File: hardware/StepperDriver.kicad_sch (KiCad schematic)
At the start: 17 parts, among them J201 Conn_01x01, J202 Conn_01x01, J203 Conn_01x01, J204 Conn_01x01, U201 TMC2130-LA

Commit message: Update parts library
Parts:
- C201, C207: footprint Capacitor_SMD:C_0603_1608Metric -> V2_Capacitor_SMD:C_0603; symbol Device:C_Small -> V2_Device:C_0603_0u1; Mouser (none) -> 810-CGA3E2X7R1H104MA
- C202: footprint Capacitor_SMD:CP_Elec_6.3x5.8 -> V2_Capacitor_SMD:CP_Elec_6.3x5.8; symbol Device:C_Polarized_Small -> V2_Device:C_Polarized_6.3x5.8_1_47u; Mouser (none) -> 667-EEE-FK1V470P
- C203, C204: footprint Capacitor_SMD:C_1210_3225Metric -> V2_Capacitor_SMD:C_1210; symbol Device:C_Small -> V2_Device:C_1210_10u; Mouser (none) -> 810-CNA6P1X7R1H106K2; Rating (none) -> 50V
- C205: footprint Capacitor_SMD:C_0603_1608Metric -> V2_Capacitor_SMD:C_0603; symbol Device:C_Small -> V2_Device:C_0603_4u7; Mouser (none) -> 603-CC603KRX5R6BB475
- C206: footprint Capacitor_SMD:C_0603_1608Metric -> V2_Capacitor_SMD:C_0603; symbol Device:C_Small -> V2_Device:C_0603_0u470; Mouser (none) -> 603-CC0603JR6BB474
- C208: footprint Capacitor_SMD:C_0603_1608Metric -> V2_Capacitor_SMD:C_0603; symbol Device:C_Small -> V2_Device:C_0603_0u022; Mouser (none) -> 603-CC603KPX7R9BB223
- J201, J202, J203, J204: value Conn_01x01 -> WAGO 2065-100
- R201: footprint Resistor_SMD:R_0603_1608Metric -> V2_Resistor_SMD:R_0603; symbol Device:R_Small -> V2_Device:R_0603_2R2; Mouser (none) -> 71-RCS06032R20JNEA
- R202, R203: footprint Resistor_SMD:R_0805_2012Metric -> V2_Resistor_SMD:R_0805; symbol Device:R_Small -> V2_Device:R_0805_0R11; Mouser (none) -> 667-ERJ-6DSFR11V

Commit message: Update parts
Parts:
- C201, C207: Manufacturer (none) -> TDK; Product (none) -> CGA3E2X7R1H104M080AA
- C202: symbol V2_Device:C_Polarized_6.3x5.8_1_47u -> V2_Device:C_Polarized_6.3x5.8_47u; Manufacturer (none) -> Panasonic; Product (none) -> EEE-FK1V470P; Rating (none) -> 35V
- C203, C204: Manufacturer (none) -> TDK; Product (none) -> CNA6P1X7R1H106K250AE; Voltage (none) -> 50V
- C205: Manufacturer (none) -> YAGEO; Product (none) -> CC0603KRX5R6BB475
- C206: value 0u470 -> 0u47; symbol V2_Device:C_0603_0u470 -> V2_Device:C_0603_0u47; Manufacturer (none) -> YAGEO; Product (none) -> CC0603JRX7R6BB474
- C208: Manufacturer (none) -> YAGEO; Product (none) -> CC0603KPX7R9BB223
- D201: LCSC (none) -> C965555; Manufacturer (none) -> Worldsemi; Product (none) -> WS2812B-2020
- J201, J202, J203, J204: Manufacturer (none) -> WAGO; Product (none) -> 2065-100/998-403
- R201: Manufacturer (none) -> Vishay; Product (none) -> RCS06032R20JNEA; Rating (none) -> 500mW
- R202, R203: Manufacturer (none) -> Panasonic; Product (none) -> ERJ-6DSFR11V; Rating (none) -> 500mW
- U201: LCSC (none) -> C915795; Manufacturer (none) -> Analog Devices; Product (none) -> TMC2130-LA
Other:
- moved on the sheet: C205, C206, R201

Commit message: Refresh
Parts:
- C201, C207: Rating (none) -> 50V
- C203, C204: Voltage 50V -> (none)
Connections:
- net +24V renamed +28V
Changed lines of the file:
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@@
 			)
 		)
-		(property "Voltage" "50V"
-			(at 158.75 68.58 0)
-			(effects
-				(font
-					(size 1.27 1.27)
-				)
-				(hide yes)
-			)
-		)
 		(property "Product" "CNA6P1X7R1H106K250AE"
 			(at 158.75 67.31 0)
@@
 			)
 		)
-		(property "Sim.Enable" ""
-			(at 158.75 49.53 0)
-			(effects
-				(font
-					(size 1.27 1.27)
-				)
-				(hide yes)
-			)
-		)
 		(pin "1"
 		)
@@
 			)
 		)
-		(property "Sim.Enable" ""
-			(at 107.95 81.28 0)
-			(effects
-				(font
-					(size 1.27 1.27)
-				)
-				(hide yes)
-			)
-		)
 		(pin "1"
 		)
@@
 	)
 	(symbol
-		(lib_id "V2_power:+24V")
+		(lib_id "V2_power:+28V")
 		(at 139.7 88.9 90)
 		(unit 1)
@@
 			)
 		)
-		(property "Value" "+24V"
+		(property "Value" "+28V"
 			(at 135.89 88.8999 90)
 			(effects
@@
 			)
 		)
-		(property "Description" "Power symbol creates a global label with name \"+24V\""
+		(property "Description" ""
 			(at 139.7 88.9 0)
 			(effects
@@
 			)
 		)
-		(property "Sim.Enable" ""
-			(at 175.26 91.44 0)
-			(effects
-				(font
-					(size 1.27 1.27)
-				)
-				(hide yes)
-			)
-		)
 		(pin "1"
 		)
@@
 			)
 		)
-		(property "Voltage" "50V"
-			(at 170.18 68.58 0)
-			(effects
-				(font
-					(size 1.27 1.27)
-				)
-				(hide yes)
-			)
-		)
 		(property "Product" "CNA6P1X7R1H106K250AE"
 			(at 170.18 67.31 0)
@@
 			)
 		)
-		(property "Sim.Enable" ""
-			(at 170.18 49.53 0)
-			(effects
-				(font
-					(size 1.27 1.27)
-				)
-				(hide yes)
-			)
-		)
 		(pin "1"
 		)
@@
 			)
 		)
-		(property "Description" "Power symbol creates a global label with name \"GND\" , ground"
+		(property "Description" ""
 			(at 191.77 129.54 0)
 			(effects
@@
 			)
 		)
-		(property "Sim.Enable" ""
-			(at 157.48 160.02 0)
-			(effects
-				(font
-					(size 1.27 1.27)
-				)
-				(hide yes)
-			)
-		)
 		(pin "1"
 		)
@@
 			)
 		)
-		(property "Sim.Enable" ""
-			(at 124.46 49.53 0)
+		(property "Rating" "50V"
+			(at 124.46 72.39 0)
 			(effects
 				(font
@@
 			)
 		)
-		(property "Description" "Power symbol creates a global label with name \"GND\" , ground"
+		(property "Description" ""
 			(at 175.26 139.7 0)
 			(effects
@@
 			)
 		)
-		(property "Description" "Power symbol creates a global label with name \"+5V\""
+		(property "Description" ""
 			(at 165.1 156.21 0)
 			(effects
@@
 			)
 		)
-		(property "Description" "Power symbol creates a global label with name \"GND\" , ground"
+		(property "Description" ""
 			(at 191.77 127 0)
 			(effects
@@
 			)
 		)
-		(property "Sim.Enable" ""
-			(at 189.23 127 90)
-			(effects
-				(font
-					(size 1.27 1.27)
-				)
-				(hide yes)
-			)
-		)
 		(pin "1"
 		)
@@
 			)
 		)
-		(property "Description" "Power symbol creates a global label with name \"GND\" , ground"
+		(property "Description" ""
 			(at 124.46 52.07 0)
 			(effects
@@
 			)
 		)
-		(property "Sim.Enable" ""
-			(at 139.7 86.36 0)
+		(property "Rating" "50V"
+			(at 139.7 109.22 0)
 			(effects
 				(font
@@
 			)
 		)
-		(property "Description" "Power symbol creates a global label with name \"GND\" , ground"
+		(property "Description" ""
 			(at 170.18 52.07 0)
 			(effects
@@
 			)
 		)
-		(property "Description" "Power symbol creates a global label with name \"GND\" , ground"
+		(property "Description" ""
 			(at 139.7 104.14 0)
 			(effects
@@
 			)
 		)
-		(property "Description" "Power symbol creates a global label with name \"+3V3\""
+		(property "Description" ""
 			(at 139.7 81.28 0)
 			(effects
@@
 			)
 		)
-		(property "Description" "Power symbol creates a global label with name \"+3V3\""
+		(property "Description" ""
 			(at 124.46 46.99 0)
 			(effects
@@
 	)
 	(symbol
-		(lib_id "V2_power:+24V")
+		(lib_id "V2_power:+28V")
 		(at 139.7 91.44 90)
 		(unit 1)
@@
 			)
 		)
-		(property "Value" "+24V"
+		(property "Value" "+28V"
 			(at 135.89 91.4399 90)
 			(effects
@@
 			)
 		)
-		(property "Description" "Power symbol creates a global label with name \"+24V\""
+		(property "Description" ""
 			(at 139.7 91.44 0)
 			(effects
@@
 			)
 		)
-		(property "Description" "Power symbol creates a global label with name \"GND\" , ground"
+		(property "Description" ""
 			(at 120.65 83.82 0)
 			(effects
@@
 			)
 		)
-		(property "Sim.Enable" ""
-			(at 143.51 49.53 0)
-			(effects
-				(font
-					(size 1.27 1.27)
-				)
-				(hide yes)
-			)
-		)
 		(pin "1"
 		)
@@
 			)
 		)
-		(property "Sim.Enable" ""
-			(at 189.23 83.82 0)
-			(effects
-				(font
-					(size 1.27 1.27)
-				)
-				(hide yes)
-			)
-		)
 		(pin "1"
 		)
@@
 			)
 		)
-		(property "Sim.Enable" ""
-			(at 189.23 81.28 0)
-			(effects
-				(font
-					(size 1.27 1.27)
-				)
-				(hide yes)
-			)
-		)
 		(pin "1"
 		)
@@
 			)
 		)
-		(property "Description" "Power symbol creates a global label with name \"GND\" , ground"
+		(property "Description" ""
 			(at 139.7 106.68 0)
 			(effects
@@
 			)
 		)
-		(property "Description" "Power symbol creates a global label with name \"GND\" , ground"
+		(property "Description" ""
 			(at 107.95 83.82 0)
 			(effects
@@
 			)
 		)
-		(property "Sim.Enable" ""
-			(at 114.3 78.74 90)
-			(effects
-				(font
-					(size 1.27 1.27)
-				)
-				(hide yes)
-			)
-		)
 		(pin "1"
 		)
@@
 			)
 		)
-		(property "Sim.Enable" ""
-			(at 157.48 106.68 0)
-			(effects
-				(font
-					(size 1.27 1.27)
-				)
-				(hide yes)
-			)
-		)
 		(pin "13"
 		)
@@
 			)
 		)
-		(property "Sim.Enable" ""
-			(at 189.23 76.2 0)
-			(effects
-				(font
-					(size 1.27 1.27)
-				)
-				(hide yes)
-			)
-		)
 		(pin "1"
 		)
@@
 			)
 		)
-		(property "Sim.Enable" ""
-			(at 189.23 129.54 90)
-			(effects
-				(font
-					(size 1.27 1.27)
-				)
-				(hide yes)
-			)
-		)
 		(pin "1"
 		)
@@
 	)
 	(symbol
-		(lib_id "V2_power:+24V")
+		(lib_id "V2_power:+28V")
 		(at 170.18 46.99 0)
 		(unit 1)
@@
 			)
 		)
-		(property "Value" "+24V"
+		(property "Value" "+28V"
 			(at 170.18 41.91 0)
 			(effects
@@
 			)
 		)
-		(property "Description" "Power symbol creates a global label with name \"+24V\""
+		(property "Description" ""
 			(at 170.18 46.99 0)
 			(effects
@@
 			)
 		)
-		(property "Sim.Enable" ""
-			(at 120.65 81.28 0)
-			(effects
-				(font
-					(size 1.27 1.27)
-				)
-				(hide yes)
-			)
-		)
 		(pin "1"
 		)
@@
 			)
 		)
-		(property "Description" "Power symbol creates a global label with name \"GND\" , ground"
+		(property "Description" ""
 			(at 139.7 124.46 0)
 			(effects
@@
 			)
 		)
-		(property "Sim.Enable" ""
-			(at 189.23 73.66 0)
-			(effects
-				(font
-					(size 1.27 1.27)
-				)
-				(hide yes)
-			)
-		)
 		(pin "1"
 		)
@@
 			)
 		)
-		(property "Description" "Power symbol creates a global label with name \"GND\" , ground"
+		(property "Description" ""
 			(at 165.1 161.29 0)
 			(effects

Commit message: Update library
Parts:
- U201: footprint V2_Driver_Stepper:QFN36-5X6 -> V2_Package_DFN_QFN:QFN36-5X6
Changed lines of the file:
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@@
 			)
 		)
-		(property "Footprint" "V2_Driver_Stepper:QFN36-5X6"
+		(property "Footprint" "V2_Package_DFN_QFN:QFN36-5X6"
 			(at 158.75 150.114 0)
 			(effects

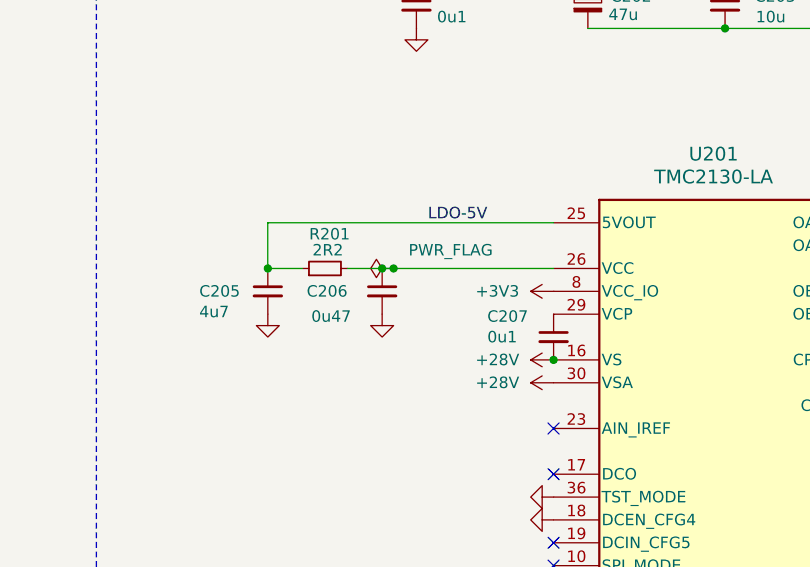
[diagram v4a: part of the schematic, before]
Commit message: Replace Order_Number
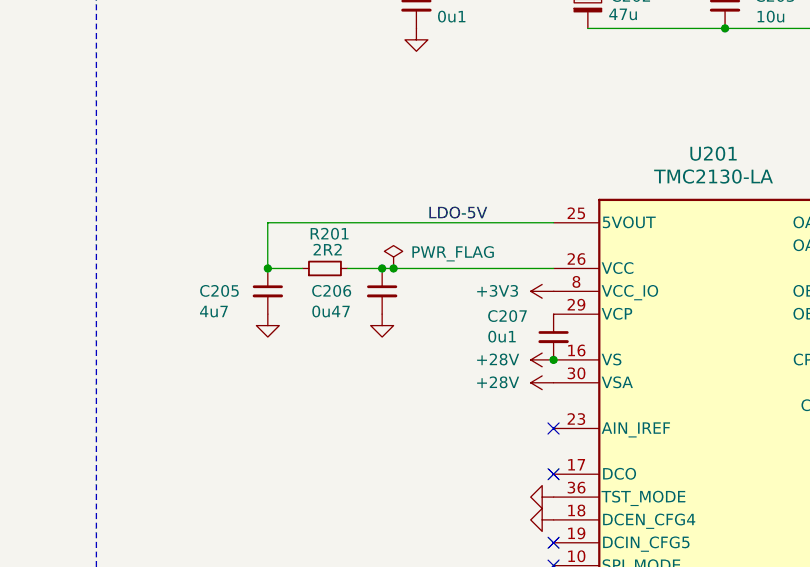
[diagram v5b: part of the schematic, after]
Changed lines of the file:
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@@
 	(title_block
 		(title "Stepper Driver")
-		(date "2025-10-27")
-		(rev "2")
+		(date "2026-02-10")
+		(rev "2026-02-10")
 		(company "Versio Duo")
 	)
@@
 		(dnp no)
 		(property "Reference" "C206"
-			(at 112.268 81.28 0)
+			(at 112.776 81.28 0)
 			(effects
 				(font
@@
 		)
 		(property "Value" "0u47"
-			(at 112.776 84.074 0)
+			(at 112.776 83.566 0)
 			(effects
 				(font
@@
 	(symbol
 		(lib_id "V2_power:PWR_FLAG")
-		(at 121.92 78.74 0)
+		(at 121.92 78.74 270)
 		(unit 1)
 		(exclude_from_sim no)
@@
 		(dnp no)
 		(property "Reference" "#FLG0201"
-			(at 121.92 76.835 0)
+			(at 123.825 78.74 0)
 			(effects
 				(font
@@
 		)
 		(property "Value" "PWR_FLAG"
-			(at 128.27 76.708 0)
+			(at 128.524 76.962 90)
 			(effects
 				(font

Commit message: Update Library
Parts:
- C201, C207: symbol V2_Device:C_0603_0u1 -> V2_Capacitor:0603_0u1
- C202: symbol V2_Device:C_Polarized_6.3x5.8_47u -> V2_Capacitor:Polarized_6.3x5.8_47u
- C203, C204: symbol V2_Device:C_1210_10u -> V2_Capacitor:1210_10u
- C205: symbol V2_Device:C_0603_4u7 -> V2_Capacitor:0603_4u7
- C206: symbol V2_Device:C_0603_0u47 -> V2_Capacitor:0603_0u47
- C208: symbol V2_Device:C_0603_0u022 -> V2_Capacitor:0603_0u022
- R201: symbol V2_Device:R_0603_2R2 -> V2_Resistor:0603_2R2
- R202, R203: symbol V2_Device:R_0805_0R11 -> V2_Resistor:0805_0R11

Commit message: Update
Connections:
- net LDO-5V renamed +5VOUT
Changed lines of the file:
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@@
 		)
 	)
-	(label "LDO-5V"
+	(label "+5VOUT"
 		(at 125.73 73.66 0)
 		(effects
@@
 		(on_board yes)
 		(dnp no)
-		(fields_autoplaced yes)
 		(property "Reference" "#PWR208"
 			(at 143.51 88.9 0)
@@
 		)
 		(property "Value" "+28V"
-			(at 135.89 88.8999 90)
-			(effects
-				(font
-					(size 1.27 1.27)
-				)
-				(justify left)
+			(at 133.35 88.8999 90)
+			(effects
+				(font
+					(size 1.27 1.27)
+					(color 255 92 187 1)
+				)
 			)
 		)
@@
 		)
 		(property "Value" "+5V"
-			(at 170.18 156.21 90)
-			(effects
-				(font
-					(size 1.27 1.27)
+			(at 171.45 156.21 90)
+			(effects
+				(font
+					(size 1.27 1.27)
+					(color 255 92 187 1)
 				)
 			)
@@
 		(on_board yes)
 		(dnp no)
-		(fields_autoplaced yes)
 		(property "Reference" "#PWR205"
 			(at 143.51 81.28 0)
@@
 		)
 		(property "Value" "+3V3"
-			(at 135.89 81.2799 90)
-			(effects
-				(font
-					(size 1.27 1.27)
-				)
-				(justify left)
+			(at 133.35 81.2799 90)
+			(effects
+				(font
+					(size 1.27 1.27)
+					(color 255 92 187 1)
+				)
 			)
 		)
@@
 				(font
 					(size 1.27 1.27)
+					(color 255 92 187 1)
 				)
 			)
@@
 		(on_board yes)
 		(dnp no)
-		(fields_autoplaced yes)
 		(property "Reference" "#PWR209"
 			(at 143.51 91.44 0)
@@
 		)
 		(property "Value" "+28V"
-			(at 135.89 91.4399 90)
-			(effects
-				(font
-					(size 1.27 1.27)
-				)
-				(justify left)
+			(at 133.35 91.4399 90)
+			(effects
+				(font
+					(size 1.27 1.27)
+					(color 255 92 187 1)
+				)
 			)
 		)
@@
 				(font
 					(size 1.27 1.27)
-				)
-			)
+					(color 255 92 187 1)
+				)
+			)

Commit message: Refresh
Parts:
- C203, C204: Mouser 810-CNA6P1X7R1H106K2 -> 810-CNC6P1X7R1H106K2; Product CNA6P1X7R1H106K250AE -> CNC6P1X7R1H106K250AE
- U201: footprint V2_Package_DFN_QFN:QFN36-5X6 -> V2_Package_DFN_QFN:QFN-36-5X6
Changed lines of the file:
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@@
 			)
 		)
-		(property "Description" "Unpolarized capacitor, small symbol"
+		(property "Description" ""
 			(at 158.75 62.992 0)
 			(effects
@@
 			)
 		)
-		(property "Mouser" "810-CNA6P1X7R1H106K2"
+		(property "Mouser" "810-CNC6P1X7R1H106K2"
 			(at 158.75 66.04 0)
 			(show_name yes)
@@
 			)
 		)
-		(property "Product" "CNA6P1X7R1H106K250AE"
+		(property "Product" "CNC6P1X7R1H106K250AE"
 			(at 158.75 67.31 0)
 			(effects
@@
 			)
 		)
-		(property "Description" "Unpolarized capacitor, small symbol"
+		(property "Description" ""
 			(at 107.95 94.742 0)
 			(effects
@@
 			)
 		)
-		(property "Description" "Unpolarized capacitor, small symbol"
+		(property "Description" ""
 			(at 175.26 104.902 0)
 			(effects
@@
 			)
 		)
-		(property "Description" "Unpolarized capacitor, small symbol"
+		(property "Description" ""
 			(at 170.18 62.992 0)
 			(effects
@@
 			)
 		)
-		(property "Mouser" "810-CNA6P1X7R1H106K2"
+		(property "Mouser" "810-CNC6P1X7R1H106K2"
 			(at 170.18 66.04 0)
 			(effects
@@
 			)
 		)
-		(property "Product" "CNA6P1X7R1H106K250AE"
+		(property "Product" "CNC6P1X7R1H106K250AE"
 			(at 170.18 67.31 0)
 			(effects
@@
 			)
 		)
-		(property "Description" "Unpolarized capacitor, small symbol"
+		(property "Description" ""
 			(at 124.46 62.992 0)
 			(effects
@@
 			)
 		)
-		(property "Description" "Resistor, small symbol"
+		(property "Description" ""
 			(at 201.422 127 0)
 			(effects
@@
 			)
 		)
-		(property "Description" "Unpolarized capacitor, small symbol"
+		(property "Description" ""
 			(at 139.7 99.822 0)
 			(effects
@@
 			)
 		)
-		(property "Description" "Polarized capacitor, small symbol"
+		(property "Description" ""
 			(at 143.51 62.738 0)
 			(effects
@@
 			)
 		)
-		(property "Description" "Resistor, small symbol"
+		(property "Description" ""
 			(at 126.492 78.74 0)
 			(effects
@@
 			)
 		)
-		(property "Footprint" "V2_Package_DFN_QFN:QFN36-5X6"
+		(property "Footprint" "V2_Package_DFN_QFN:QFN-36-5X6"
 			(at 158.75 150.114 0)
 			(effects
@@
 			)
 		)
-		(property "Description" "Resistor, small symbol"
+		(property "Description" ""
 			(at 201.422 129.54 0)
 			(effects
@@
 			)
 		)
-		(property "Description" "Unpolarized capacitor, small symbol"
+		(property "Description" ""
 			(at 120.65 94.742 0)
 			(effects
